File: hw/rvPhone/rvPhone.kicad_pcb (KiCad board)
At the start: 4 copper layers, 135 x 70 mm, 235 parts, among them J1 USB_OTG, J2 BATT, J202 Modem, J203 SIM_Card, J204 Motor, J205 Micro_SD_Card, J206 Camera, J3 SJ-3571N, J301 iMX8, J302 Touch, J303 Display, J304 Prog, Q1 MMBT3906, SW1 RESET, SW2 WAKE, SW201 BOOT, U1 BQ25895, U10 74HC595, U11 ICS-43434, U12 MAX98357A, U13 FT813Q, U14 FAN5333BSX, U2 TPS62293, U201 ESP32-WROOM, U202 SN74CBTLV3125, U203 TXB0104RGY, U204 TXB0104RGY, U205 DRV2605L, U206 SN74CBTLV3126, U207 TPS22917, U208 SN74LVC2G66, U209 TPS22917, U3 TPS630250, U301 SN65LVDS822_SWAP, U302 TS3DDR3812, U303 TS3DDR3812, U304 TS3DDR3812, U4 TMUX154E, U5 E310-G002, U6 IS25LP128-JBLE, U7 74HC00, U8 74HC00, U9 74HC595, X1 SiT1533, Y1 16MHz, Y2 12MHz

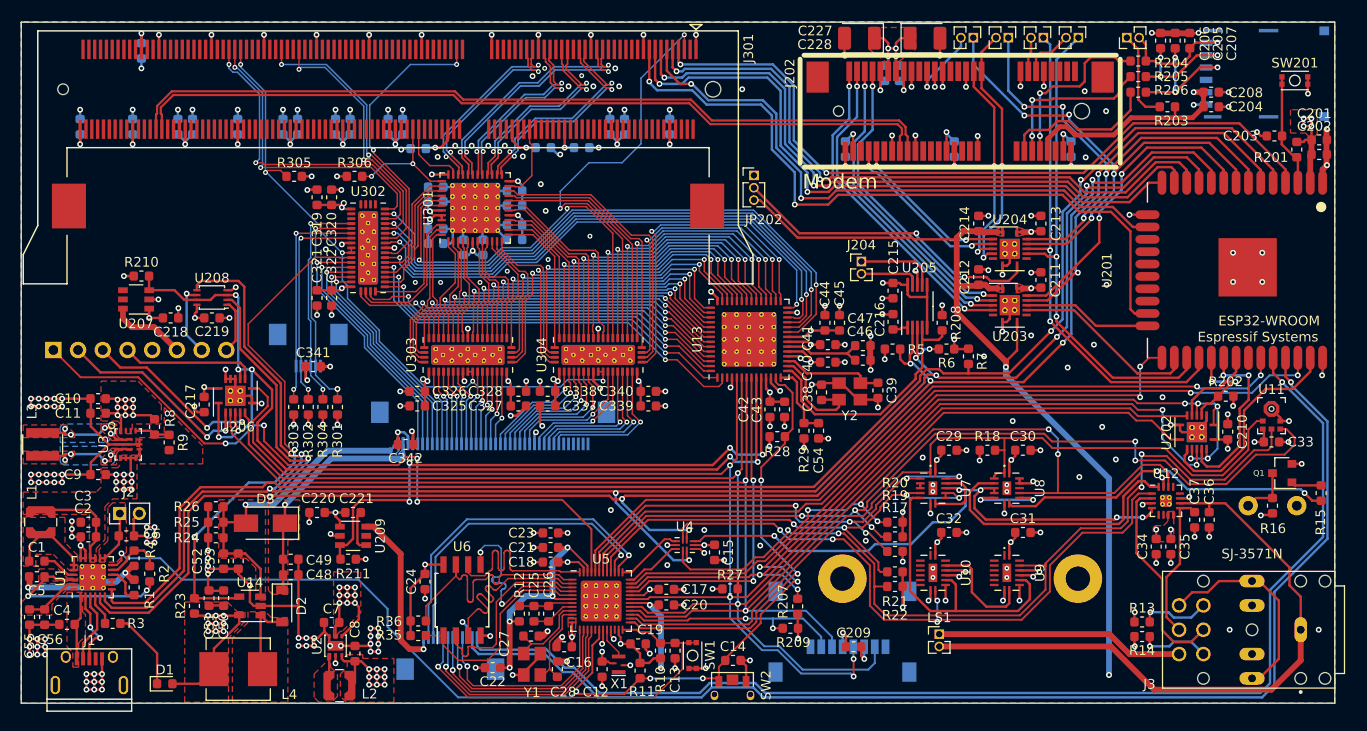
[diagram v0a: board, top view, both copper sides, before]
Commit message: stereo audio out; lvds display; LSM9DS1 added
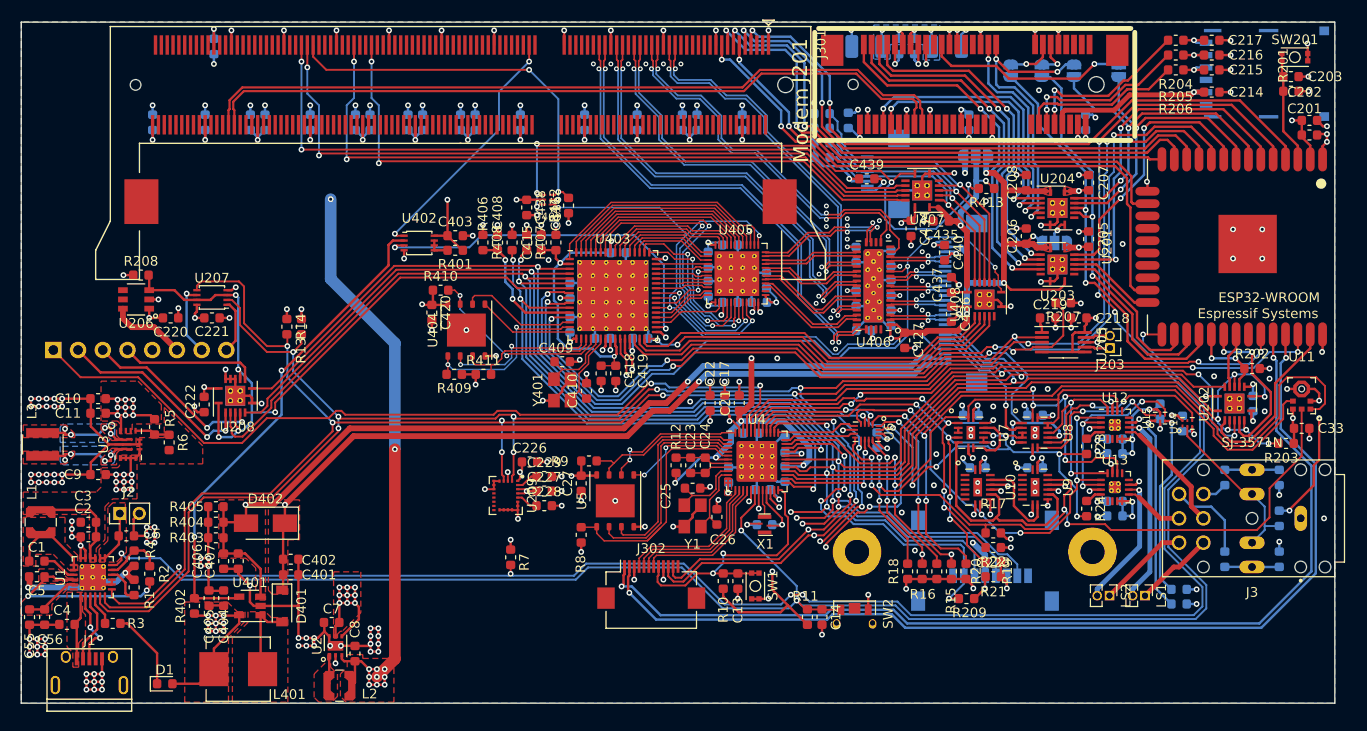
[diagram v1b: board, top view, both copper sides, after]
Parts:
- removed BZ1: Buzzer, footprints:Buzzer_12x9.5RM5.0
- removed the C15 at (168.4, 126.3)
- removed the C18 at (151.6, 127.3)
- removed the C208 at (219.5, 79.0)
- removed the C220 at (127.6, 122.2)
- removed the C221 at (131.3, 122.2)
- removed the C222 at (185.9, 77.0)
- removed the C223 at (187.4, 77.0)
- removed the C224 at (205.1, 84.8)
- removed the C225 at (193.1, 84.8)
- removed C319, C321, C325, C327, C337, C339: 1uF, Capacitor_SMD:C_0603_1608Metric
- removed C320, C322, C323, C326, C328, C329, C331, C333, C335, C338, C340, C342: 0.1uF, Capacitor_SMD:C_0603_1608Metric
- removed C324, C330, C332, C334, C336: 0.01uF, Capacitor_SMD:C_0603_1608Metric
- removed the J202 at (206.2, 81.0)
- removed the J302 at (126.7, 105.3)
- removed J303: Display, Connector_FFC-FPC:Hirose_FH12-40S-0.5SH_1x40-1MP_P0.50mm_Horizontal
- removed JP206: Q.RXD, Connector_PinHeader_1.27mm:PinHeader_1x02_P1.27mm_Vertical
- removed Q1: MMBT3906, Package_TO_SOT_SMD:SOT-23
- removed the R13 at (212.4, 133.4)
- removed the R14 at (212.4, 134.9)
- removed the R203 at (215.0, 80.5)
- removed R211, R306: 100K, Resistor_SMD:R_0603_1608Metric
- removed R302: 1K, Resistor_SMD:R_0603_1608Metric
- removed R305: 47K, Resistor_SMD:R_0603_1608Metric
- removed the U207 at (109.0, 100.3)
- removed U301: SN65LVDS822_SWAP, Package_DFN_QFN:QFN-48-1EP_7x7mm_P0.5mm_EP5.15x5.15mm_ThermalVias
- removed U302, U303, U304: TS3DDR3812, footprints:Texas_R-PWQFN-N42
- removed the U4 at (165.4, 125.5)
- removed Y2: 12MHz, footprints:TXC_7M
- added C17: 0.1uF, Capacitor_SMD:C_0603_1608Metric, F.Cu at (169.5, 111.0)
- added C209: 0.1uF, Capacitor_SMD:C_0603_1608Metric, B.Cu at (206.6, 82.1)
- added C210: 0.1uF, Capacitor_SMD:C_0603_1608Metric, B.Cu at (194.6, 82.1)
- added C211: 0.1uF, Capacitor_SMD:C_0603_1608Metric, B.Cu at (182.2, 81.9)
- added C212: 0.1uF, Capacitor_SMD:C_0603_1608Metric, B.Cu at (187.4, 74.3)
- added C213: 0.1uF, Capacitor_SMD:C_0603_1608Metric, B.Cu at (189.0, 74.3)
- added C227: 0.1uF, Capacitor_SMD:C_0603_1608Metric, F.Cu at (150.9, 120.0)
- added C228: 0.01uF, Capacitor_SMD:C_0603_1608Metric, F.Cu at (150.9, 121.5)
- added C229: 0.1uF, Capacitor_SMD:C_0603_1608Metric, F.Cu at (150.9, 118.5)
- added C26: 12pF, Capacitor_SMD:C_0603_1608Metric, F.Cu at (168.7, 122.7)
- added C40: 0.1uF, Capacitor_SMD:C_0603_1608Metric, B.Cu at (216.6, 113.0)
- added C403: 0.1uF, Capacitor_SMD:C_0603_1608Metric, F.Cu at (141.8, 93.8)
- added C409: 18pF, Capacitor_SMD:C_0603_1608Metric, F.Cu at (152.8, 106.7)
- added C41: 0.1uF, Capacitor_SMD:C_0603_1608Metric, B.Cu at (214.2, 111.8)
- added C410: 18pF, Capacitor_SMD:C_0603_1608Metric, F.Cu at (155.3, 109.7)
- added C415: 1uF, Capacitor_SMD:C_0603_1608Metric, F.Cu at (150.7, 94.5)
- added C420: 0.1uF, Capacitor_SMD:C_0603_1608Metric, F.Cu at (139.4, 101.7)
- added C421: 0.01uF, Capacitor_SMD:C_0603_1608Metric, B.Cu at (167.8, 99.2)
- added C422: 0.1uF, Capacitor_SMD:C_0603_1608Metric, B.Cu at (170.1, 100.6)
- added C423: 0.01uF, Capacitor_SMD:C_0603_1608Metric, B.Cu at (173.1, 100.6)
- added C424: 0.1uF, Capacitor_SMD:C_0603_1608Metric, B.Cu at (173.8, 98.3)
- added C425: 0.01uF, Capacitor_SMD:C_0603_1608Metric, B.Cu at (167.8, 96.2)
- added C426: 0.1uF, Capacitor_SMD:C_0603_1608Metric, B.Cu at (170.1, 94.7)
- added C427: 0.1uF, Capacitor_SMD:C_0603_1608Metric, F.Cu at (188.0, 104.5)
- added C428: 0.1uF, Capacitor_SMD:C_0603_1608Metric, B.Cu at (186.6, 102.2)
- added C429: 0.1uF, Capacitor_SMD:C_0603_1608Metric, B.Cu at (186.6, 99.1)
- added C430: 0.1uF, Capacitor_SMD:C_0603_1608Metric, B.Cu at (186.6, 96.1)
- added C431: 0.1uF, Capacitor_SMD:C_0603_1608Metric, B.Cu at (183.0, 95.7)
- added C432: 0.1uF, Capacitor_SMD:C_0603_1608Metric, B.Cu at (183.0, 100.2)
- added C433: 0.1uF, Capacitor_SMD:C_0603_1608Metric, B.Cu at (183.8, 103.5)
- added C434: 0.1uF, Capacitor_SMD:C_0603_1608Metric, F.Cu at (188.7, 93.0)
- added C435: 0.1uF, Capacitor_SMD:C_0603_1608Metric, F.Cu at (191.8, 92.2)
- added C436: 0.1uF, Capacitor_SMD:C_0603_1608Metric, F.Cu at (192.8, 101.8)
- added C437: 0.1uF, Capacitor_SMD:C_0603_1608Metric, F.Cu at (192.8, 98.8)
- added C438: 0.1uF, Capacitor_SMD:C_0603_1608Metric, F.Cu at (149.2, 90.8)
- added C440: 0.1uF, Capacitor_SMD:C_0603_1608Metric, F.Cu at (192.1, 95.5)
- added J201: Modem, footprints:Socket_mPCIe, F.Cu at (207.7, 78.2)
- added J401: Touch, Connector_FFC-FPC:Hirose_FH12-8S-0.5SH_1x08-1MP_P0.50mm_Horizontal, B.Cu at (186.0, 87.4)
- added J402: Display, Connector_FFC-FPC:Hirose_FH12-26S-0.5SH_1x26-1MP_P0.50mm_Horizontal, B.Cu at (194.0, 100.7)
- added JP401: CTP_PWR, Jumper:SolderJumper-3_P1.3mm_Open_RoundedPad1.0x1.5mm, B.Cu at (195.3, 85.6)
- added LS2: Speaker, Connector_PinHeader_1.27mm:PinHeader_1x02_P1.27mm_Vertical, F.Cu at (209.1, 130.8)
- added R23: 2K, Resistor_SMD:R_0603_1608Metric, F.Cu at (206.7, 115.4)
- added R24: 210K, Resistor_SMD:R_0603_1608Metric, F.Cu at (206.7, 121.8)
- added R25: 47K, Resistor_SMD:R_0603_1608Metric, B.Cu at (226.5, 127.0)
- added R26: 47K, Resistor_SMD:R_0603_1608Metric, B.Cu at (226.5, 118.6)
- added R28: 100K, Resistor_SMD:R_0603_1608Metric, B.Cu at (216.2, 131.6)
- added R29: 100K, Resistor_SMD:R_0603_1608Metric, B.Cu at (216.2, 130.1)
- added R401: 47K, Resistor_SMD:R_0603_1608Metric, F.Cu at (141.8, 95.2)
- added R407: 47K, Resistor_SMD:R_0603_1608Metric, F.Cu at (149.2, 94.5)
- added R409: 47K, Resistor_SMD:R_0603_1608Metric, F.Cu at (141.7, 108.0)
- added R410: 47K, Resistor_SMD:R_0603_1608Metric, F.Cu at (140.3, 99.3)
- added R411: 47K, Resistor_SMD:R_0603_1608Metric, F.Cu at (144.7, 108.0)
- added R412: 47K, Resistor_SMD:R_0603_1608Metric, F.Cu at (153.4, 90.7)
- added R413: 47K, Resistor_SMD:R_0603_1608Metric, F.Cu at (196.4, 88.9)
- added R415: 1K, Resistor_SMD:R_0603_1608Metric, B.Cu at (179.5, 84.2)
- added U14: SN74LVC1G04DRY, footprints:USON-6_1.45x1mm_P0.5mm, F.Cu at (217.1, 113.0)
- added U15: SN74LVC1G3157DRY, footprints:USON-6_1.45x1mm_P0.5mm, F.Cu at (214.2, 112.5)
- added U206: TPS22917, footprints:TPS22917, F.Cu at (109.0, 100.3)
- added U402: SN74LVC3G06DCU, Package_SO:VSSOP-8_2.4x2.1mm_P0.5mm, F.Cu at (138.1, 94.5)
- added U403: BT815Q, Package_DFN_QFN:QFN-64-1EP_9x9mm_P0.5mm_EP7.3x7.3mm_ThermalVias, F.Cu at (158.0, 99.9)
- added U404: IS25LP128-JKLE, Package_SON:WSON-8-1EP_6x5mm_P1.27mm_EP3.4x4mm, F.Cu at (142.9, 103.5)
- added U405: DS90C185, Package_DFN_QFN:QFN-48-1EP_6x6mm_P0.4mm_EP4.6x4.6mm_ThermalVias, F.Cu at (170.8, 97.7)
- added U406: TS3DV520E, footprints:Texas_R-PWQFN-N42, F.Cu at (184.8, 98.9)
- added U407: TXS0104ERGY, Package_DFN_QFN:Texas_S-PVQFN-N14_ThermalVias, F.Cu at (189.8, 89.1)
- added U408: TXS0104ERGY, Package_DFN_QFN:Texas_S-PVQFN-N14_ThermalVias, F.Cu at (196.2, 100.3)
- added U409: SN74LVC2G06DRY, footprints:USON-6_1.45x1mm_P0.5mm, F.Cu at (151.3, 90.0)
- added U5: IS25LP128-JKLE, Package_SON:WSON-8-1EP_6x5mm_P1.27mm_EP3.4x4mm, F.Cu at (158.2, 121.0)
- added Y401: 12MHz, footprints:TXC_7M, F.Cu at (152.8, 109.6)
- C12, C29, C30, C31, C32: moved to B.Cu
- C15: renamed from C16; moved to B.Cu
- C16: renamed from C17; moved to B.Cu
- C18: renamed from C19; moved to B.Cu
- C19: renamed from C20; moved to B.Cu
- C20: renamed from C21; moved to B.Cu
- C204: renamed from C210; moved to B.Cu
- C224: renamed from C227; moved to B.Cu
- C225: renamed from C228; moved to B.Cu
- C226: moved to F.Cu
- C28: value 12pF -> 0.1uF; moved to B.Cu
- C34: renamed from C35; moved to B.Cu
- C35: renamed from C34; moved to B.Cu
- C36: value 220pF -> 0.1uF; moved to B.Cu
- C37: value 220pF -> 10uF; moved to B.Cu
- C38, C39: value 18pF -> 10uF; moved to B.Cu
- C411: renamed from C40; moved to B.Cu
- C412: renamed from C41; moved to B.Cu
- C413: renamed from C42; value 27pF -> 0.1uF; moved to B.Cu
- C414: renamed from C43; moved to B.Cu
- C416: renamed from C44; value 27pF -> 0.1uF
- C417: renamed from C45; moved to B.Cu
- C418: renamed from C46; value 4.7uF -> 10uF
- J205: footprint footprints:MicroSd -> footprints:microSD
- J3: footprint footprints:CUI_SJ-3571N -> footprints:SJ-3571N
- J302: renamed from J304; moved to F.Cu
- JP201: value SIM PULL -> LEVEL EN; footprint Connector_PinHeader_1.27mm:PinHeader_1x02_P1.27mm_Vertical -> Jumper:SolderJumper-3_P1.3mm_Open_RoundedPad1.0x1.5mm; moved to B.Cu
- JP202: value LEVEL EN -> Q.DTR; footprint Connector_PinHeader_1.27mm:PinHeader_1x03_P1.27mm_Vertical -> Jumper:SolderJumper-2_P1.3mm_Open_RoundedPad1.0x1.5mm; moved to B.Cu
- JP203: value Q.DTR -> Q.RI; footprint Connector_PinHeader_1.27mm:PinHeader_1x02_P1.27mm_Vertical -> Jumper:SolderJumper-2_P1.3mm_Open_RoundedPad1.0x1.5mm; moved to B.Cu
- JP204: value Q.RI -> Q.TXD; footprint Connector_PinHeader_1.27mm:PinHeader_1x02_P1.27mm_Vertical -> Jumper:SolderJumper-2_P1.3mm_Open_RoundedPad1.0x1.5mm; moved to B.Cu
- JP205: value Q.TXD -> Q.RXD; footprint Connector_PinHeader_1.27mm:PinHeader_1x02_P1.27mm_Vertical -> Jumper:SolderJumper-2_P1.3mm_Open_RoundedPad1.0x1.5mm; moved to B.Cu
- R15, R16: value 1K -> 100K
- R27: value 47K -> 100K; moved to B.Cu
- R414: renamed from R301; value 4.7K -> 10K; moved to B.Cu
- R416: renamed from R303; moved to B.Cu
- R417: renamed from R304; moved to B.Cu
- U11: footprint footprints:TDK_ICS-43434 -> footprints:ICS-43434
- U13: value FT813Q -> MAX98357A; footprint Package_DFN_QFN:QFN-56-1EP_8x8mm_P0.5mm_EP5.6x5.6mm_ThermalVias -> footprints:TQFN-16-1EP_3x3mm_P0.5mm_EP1.23x1.23mm_ThermalVias
- U202: value SN74CBTLV3125 -> SN74CBTLV3125RGY
- U207: renamed from U208; value SN74LVC2G66 -> SN74LVC2G66DCU
- U208: renamed from U206; value SN74CBTLV3126 -> SN74CBTLV3126RGY
- U209: value TPS22917 -> LSM9DS1; footprint footprints:Texas_R-PDSO-G6 -> Package_LGA:LGA-24L_3x3.5mm_P0.43mm
- U6: value IS25LP128-JBLE -> TMUX1574RSV; footprint Package_SO:SOIJ-8_5.3x5.3mm_P1.27mm -> footprints:UQFN-16_1.8x2.6mm_P0.4mm
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- renumbered C211 to C205, C212 to C206, C213 to C207, C214 to C208, C22 to C21, C204 to C214, C205 to C215, C206 to C216, C207 to C217, C215 to C218, C216 to C219, C23 to C22, C218 to C220, C219 to C221, C217 to C222, C209 to C223, C25 to C23, C26 to C24, C27 to C25, C24 to C27, C48 to C401, C49 to C402, C50 to C404, C51 to C405, C52 to C406, C53 to C407, C54 to C408, C47 to C419, C341 to C439, D2 to D401, D3 to D402, J203 to J202, J204 to J203, J206 to J204, L4 to L401, R5 to R13, R6 to R14, R207 to R203, R208 to R207, R210 to R208, R23 to R402, R24 to R403, R25 to R404, R26 to R405, R29 to R406, R28 to R408, R8 to R5, R9 to R6, R35 to R8, R36 to R9, U5 to U4, U14 to U401
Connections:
- net BL_PWM renamed Net-(R402-Pad2)
- C217 pad 1: Net-(C207-Pad1) -> Net-(C217-Pad1)
- C28 pad 1: /XTAL_XO -> +3V3
- C34 pad 1: +3V3 -> +VSYS
- C35 pad 1: +3V3 -> +VSYS
- C36 pad 1: /SPK_VO- -> +VSYS
- C37 pad 1: /SPK_VO+ -> +VSYS
- C38 pad 2: GND -> Net-(C38-Pad2)
- C39 pad 2: GND -> Net-(C39-Pad2)
- C408 pad 1: Net-(C54-Pad1) -> Net-(C408-Pad1)
- C414 pad 1: +3V3 -> +1V8
- C416 pad 1: +3V3 -> /disp/BT81X_1V2
- C417 pad 1: +3V3 -> /disp/BT81X_1V2
- C418 pad 1: Net-(C46-Pad1) -> /disp/BT81X_1V2
- C419 pad 1: Net-(C46-Pad1) -> /disp/BT81X_1V2
- J202 pad 7: Net-(C207-Pad1) -> Net-(C217-Pad1)
- J205 pad 2: SPI1.SS0 -> SPI1.SS3
- J3 pad 1: /SPK_VO- -> GND
- J3 pad 10: Net-(J3-Pad10) -> /HP_DET
- J3 pad 11: Net-(J3-Pad11) -> /HP_DET
- J3 pad 2: Net-(J3-Pad2) -> Net-(C39-Pad1)
- J3 pad 3: Net-(J3-Pad2) -> Net-(C38-Pad1)
- J3 pad 4: Net-(J3-Pad4) -> /SPK_L+
- J3 pad 5: /SPK_GAIN -> /SPK_L_HP+
- J3 pad 6: Net-(J3-Pad6) -> Net-(C39-Pad2)
- J3 pad 7: /EAR_VO+ -> /SPK_R+
- J3 pad 8: /SPK_VO+ -> /SPK_R_HP_+
- J3 pad 9: Net-(J3-Pad2) -> Net-(C38-Pad2)
- J301 pad 129: iMX8_I2C1_SCL -> iMX8.I2C1.SCL
- J301 pad 135: iMX8_I2C1_SDA -> iMX8.I2C1.SDA
- J301 pad 149: iMX8_GPIO3_IO13 -> iMX8.GPIO3.IO13
- J301 pad 151: iMX8_GPIO3_IO12 -> iMX8.GPIO3.IO12
- J301 pad 153: iMX8_GPIO3_IO11 -> iMX8.GPIO3.IO11
- J301 pad 176: iMX8_USB1_D_P -> iMX8.USB1.D_P
- J301 pad 178: iMX8_USB1_D_N -> iMX8.USB1.D_N
- J301 pad 33: iMX8_LVDS0_CLK_P -> iMX8.LVDS0.CLK_P
- J301 pad 35: iMX8_LVDS0_CLK_N -> iMX8.LVDS0.CLK_N
- J301 pad 39: iMX8_LVDS0_A0_P -> iMX8.LVDS0.A0_P
- J301 pad 41: iMX8_LVDS0_A0_N -> iMX8.LVDS0.A0_N
- J301 pad 45: iMX8_LVDS0_A1_P -> iMX8.LVDS0.A1_P
- J301 pad 47: iMX8_LVDS0_A1_N -> iMX8.LVDS0.A1_N
- J301 pad 5: iMX8_GPIO5_IO28 -> Net-(J301-Pad5)
- J301 pad 51: iMX8_LVDS0_A2_P -> iMX8.LVDS0.A2_P
- J301 pad 53: iMX8_LVDS0_A2_N -> iMX8.LVDS0.A2_N
- J301 pad 57: iMX8_LVDS0_A3_P -> iMX8.LVDS0.A3_P
- J301 pad 58: iMX8_GPIO5_IO25 -> Net-(J301-Pad58)
- J301 pad 59: iMX8_LVDS0_A3_N -> iMX8.LVDS0.A3_N
- J301 pad 75: iMX8_PWM1 -> iMX8.PWM1
- J301 pad 88: iMX8_GPIO2_IO17 -> Net-(J301-Pad88)
- J301 pad 90: iMX8_GPIO2_IO18 -> Net-(J301-Pad90)
- J302 pad 12: TPS.VOUT -> Net-(J302-Pad12)
- JP201 pad 1: Net-(JP201-Pad1) -> GND
- JP201 pad 2: Net-(C207-Pad1) -> Net-(JP201-Pad2)
- JP202 pad 1: GND -> /periph/ESP32.U2.DTR
- JP202 pad 2: Net-(JP202-Pad2) -> /periph/Quectel.UART.DTR
- JP203 pad 1: /periph/ESP32.U2.DTR -> /periph/ESP32.U2.RI
- JP203 pad 2: /periph/Quectel.UART.DTR -> /periph/Quectel.UART.RI
- JP204 pad 1: /periph/ESP32.U2.RI -> /periph/ESP32.U2.RXD
- JP204 pad 2: /periph/Quectel.UART.RI -> /periph/Quectel.UART.TXD
- JP205 pad 1: /periph/ESP32.U2.RXD -> /periph/ESP32.U2.TXD
- JP205 pad 2: /periph/Quectel.UART.TXD -> /periph/Quectel.UART.RXD
- LS1 pad 1: /EAR_VO+ -> /SPK_L+
- LS1 pad 2: /SPK_VO- -> /SPK_L-
- R15 pad 1: Net-(Q1-Pad1) -> TMUX.GPIO0
- R15 pad 2: Net-(R15-Pad2) -> GND
- R16 pad 1: Net-(BZ1-Pad1) -> TMUX.GPIO1
- R18 pad 2: PWM0.1 -> /MIC_CLK
- R19 pad 2: PWM1.1 -> /MIC_WS
- R203 pad 2: SPI1.SS3 -> SPI1.SS0
- R204 pad 1: Net-(C207-Pad1) -> Net-(C217-Pad1)
- R207 pad 2: FT813.GPIO3 -> BT81X.GPIO3
- R208 pad 2: FT813.GPIO0 -> BT81X.GPIO0
- R209 pad 2: SPI1.SS0 -> SPI1.SS3
- R22 pad 2: /I2S_SD_OUT -> /MIC_SD
- R27 pad 1: +3V3 -> /HP_DET
- R27 pad 2: SPI1.SS2 -> +3V3
- R406 pad 2: Net-(C54-Pad1) -> Net-(C408-Pad1)
- R414 pad 2: /exp/CTP_INT -> /disp/CTP_INT
- R416 pad 2: /exp/CTP_SCL -> /disp/CTP_SCL
- R417 pad 1: /exp/CTP_RST -> /disp/CTP_RST
- U10 pad 9: /I2S_SD_IN -> /SPK_SD
- U11 pad 1: PWM1.1 -> /MIC_WS
- U11 pad 4: PWM0.1 -> /MIC_CLK
- U11 pad 6: /I2S_SD_OUT -> /MIC_SD
- U12 pad 1: /I2S_SD_IN -> /SPK_SD
- U12 pad 10: /SPK_VO- -> /SPK_L-
- U12 pad 4: /SPK_EN -> Net-(R23-Pad1)
- U12 pad 7: +3V3 -> +VSYS
- U12 pad 8: +3V3 -> +VSYS
- U12 pad 9: /SPK_VO+ -> /SPK_L_HP+
- U13 pad 1: FT813_R1 -> /SPK_SD
- U13 pad 10: FT813.GPIO1 -> /SPK_R-
- U13 pad 11: +3V3 -> GND
- U13 pad 12: Net-(U13-Pad12) -> (no net)
- U13 pad 13: GPIO_0 -> (no net)
- U13 pad 14: Net-(C54-Pad1) -> PWM2.1
- U13 pad 15: FT813.GPIO3 -> GND
- U13 pad 16: Net-(C38-Pad1) -> /SPK_CLK
- U13 pad 17: Net-(C39-Pad1) -> GND
- U13 pad 2: FT813_R0 -> /SPK_GAIN
- U13 pad 3: Net-(U13-Pad3) -> GND
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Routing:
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- added copper zone on B.Cu, net +3V3
- removed copper zone on B.Cu, net DISP_LED_A
- removed copper zone on B.Cu, net DISP_LED_K
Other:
- net class AUDIO added: clearance 0.2, trace_width 0.2, via_dia 0.6, via_drill 0.3
- net class BT81X added: clearance 0.1524, trace_width 0.1524, via_dia 0.508, via_drill 0.254
- net class CTP added: clearance 0.2, trace_width 0.2, via_dia 0.6, via_drill 0.3
- net class FE310: via_dia 0.6096 -> 0.508; via_drill 0.3048 -> 0.254

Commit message: rev2 board
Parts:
- removed the C221 at (116.8, 102.2)
- removed the C222 at (116.0, 111.1)
- removed C405, C407: 27pF, Capacitor_SMD:C_0603_1608Metric
- removed C55, C56: 22uF, Capacitor_SMD:C_0603_1608Metric
- removed J302: Prog, Connector_FFC-FPC:Hirose_FH12-12S-0.5SH_1x12-1MP_P0.50mm_Horizontal
- removed LS1, LS2: Speaker, Connector_PinHeader_1.27mm:PinHeader_1x02_P1.27mm_Vertical
- removed the R208 at (109.5, 97.8)
- removed the R414 at (179.5, 82.7)
- removed R417: 100K, Resistor_SMD:R_0603_1608Metric
- removed U209: LSM9DS1, Package_LGA:LGA-24L_3x3.5mm_P0.43mm
- added C218: 470uF, Capacitor_Tantalum_SMD:CP_EIA-7343-31_Kemet-D, B.Cu at (182.4, 74.4)
- added C219: 10nF, Capacitor_SMD:C_0603_1608Metric, F.Cu at (226.4, 78.7)
- added C230: 0.1uF, Capacitor_SMD:C_0603_1608Metric, F.Cu at (153.6, 117.9)
- added C319: 0.1uF, Capacitor_SMD:C_0603_1608Metric, F.Cu at (111.3, 86.7)
- added C42: 10uF, Capacitor_SMD:C_0603_1608Metric, F.Cu at (111.2, 127.2)
- added C43: 22uF, Capacitor_SMD:C_0805_2012Metric, F.Cu at (108.0, 124.3)
- added C44: 22uF, Capacitor_SMD:C_0805_2012Metric, F.Cu at (108.0, 126.3)
- added C441: 10uF, Capacitor_SMD:C_0603_1608Metric, F.Cu at (166.2, 102.0)
- added C45: 0.1uF, Capacitor_SMD:C_0603_1608Metric, F.Cu at (133.6, 117.8)
- added J206: Expansion, Connector_Molex:Molex_SlimStack_54722-0164_2x08_P0.50mm_Vertical, F.Cu at (168.4, 131.1)
- added J207: Camera, Connector_Molex:Molex_SlimStack_54722-0164_2x08_P0.50mm_Vertical, B.Cu at (110.6, 97.1)
- added J305: Micro_SD_Card, footprints:microSD, B.Cu at (113.3, 81.7)
- added J4: SJ-3571N, footprints:SJ-3571N, F.Cu at (223.5, 123.0)
- added J5: SPEAKER, Connector_PinHeader_2.54mm:PinHeader_1x04_P2.54mm_Vertical, F.Cu at (214.3, 132.4)
- added JP301: ALT_BOOT, Jumper:SolderJumper-2_P1.3mm_Open_RoundedPad1.0x1.5mm, B.Cu at (107.7, 91.0)
- added JP402: VOD_SEL, Jumper:SolderJumper-3_P1.3mm_Open_RoundedPad1.0x1.5mm, B.Cu at (168.4, 91.3)
- added R209: 4.7K, Resistor_SMD:R_0603_1608Metric, F.Cu at (149.9, 120.5)
- added R210: 10K, Resistor_SMD:R_0603_1608Metric, F.Cu at (151.4, 120.5)
- added R418: 100K, Resistor_SMD:R_0603_1608Metric, F.Cu at (148.9, 94.7)
- added SW202: PERST, Button_Switch_SMD:SW_SPST_PTS810, F.Cu at (225.6, 75.1)
- added TP1: BQ_INT, TestPoint:TestPoint_Pad_D1.5mm, B.Cu at (116.2, 126.6)
- added TP401: AUDIO, TestPoint:TestPoint_Pad_D1.5mm, F.Cu at (160.9, 107.2)
- added U16: SN74LVC2G07DCK, Package_TO_SOT_SMD:Texas_R-PDSO-G6, F.Cu at (136.7, 117.8)
- C10: value 22uF -> 10uF
- C11: value 22uF -> 47uF; footprint Capacitor_SMD:C_0603_1608Metric -> Capacitor_SMD:C_0805_2012Metric
- C202: value 10uF -> 22uF; footprint Capacitor_SMD:C_0603_1608Metric -> Capacitor_SMD:C_0805_2012Metric
- C203: value 0.1uF -> 1uF
- C220: value 1uF -> 10nF
- C224: value 470uF -> 0.1uF; footprint Capacitor_Tantalum_SMD:CP_EIA-3528-21_Kemet-B -> Capacitor_SMD:C_0603_1608Metric; moved to F.Cu
- C225: value 470uF -> 0.01uF; footprint Capacitor_Tantalum_SMD:CP_EIA-3528-21_Kemet-B -> Capacitor_SMD:C_0603_1608Metric; moved to F.Cu
- C228: value 0.01uF -> 0.1uF
- C25, C26: value 12pF -> 10pF
- C311, C312, C313: moved to F.Cu
- C314, C315, C316, C317, C318: footprint Capacitor_SMD:C_0603_1608Metric -> Capacitor_SMD:C_0805_2012Metric
- C409, C410: value 18pF -> 10pF
- C427, D1: moved to B.Cu
- J2: footprint Connector_PinHeader_2.00mm:PinHeader_1x02_P2.00mm_Vertical -> Connector_PinHeader_2.54mm:PinHeader_1x02_P2.54mm_Vertical
- J203: footprint Connector_PinHeader_1.27mm:PinHeader_1x02_P1.27mm_Vertical -> footprints:SolderWirePad_1x02_SMD_1x2mm; moved to B.Cu
- J204: value Camera -> Micro_SD_Card; footprint Connector_PinHeader_2.54mm:PinHeader_1x08_P2.54mm_Vertical -> footprints:microSD
- J205: value Micro_SD_Card -> Prog; footprint footprints:microSD -> Connector_FFC-FPC:Hirose_FH12-12S-0.5SH_1x12-1MP_P0.50mm_Horizontal; moved to F.Cu
- J3: value SJ-3571N -> +5V; footprint footprints:SJ-3571N -> Connector_PinHeader_2.54mm:PinHeader_1x02_P2.54mm_Vertical
- L1: footprint footprints:L_Coilcraft_LPS3015 -> Inductor_SMD:L_Vishay_IHLP-1616
- R23: value 2K -> 2.2K
- R24: value 210K -> 255K
- R28, R29: value 100K -> 50K
- R405: value R -> 68R
- R414: renamed from R415; value 1K -> R
- R415: renamed from R416; value 1K -> R
- R7: value 10K -> 100K
- SW1, SW201: footprint footprints:Panasonic_EVPBB -> Button_Switch_SMD:SW_SPST_PTS810
- SW2: footprint footprints:Panasonic_EVPAK -> footprints:Panasonic_EVPAE
- U14: value SN74LVC1G04DRY -> SN74LVC1G04DCK; footprint footprints:USON-6_1.45x1mm_P0.5mm -> footprints:Texas_R-PDSO-G5
- U15: value SN74LVC1G3157DRY -> SN74LVC1G3157DCK; footprint footprints:USON-6_1.45x1mm_P0.5mm -> Package_TO_SOT_SMD:Texas_R-PDSO-G6
- U205: value DRV2605L -> DRV2605LDGS
- U206: value TPS22917 -> LSM9DS1; footprint footprints:TPS22917 -> Package_LGA:LGA-24L_3x3.5mm_P0.43mm
- U207: value SN74LVC2G66DCU -> FT230XQ; footprint Package_SO:VSSOP-8_2.4x2.1mm_P0.5mm -> Package_DFN_QFN:QFN-16-1EP_4x4mm_P0.65mm_EP2.1x2.1mm
- U208: value SN74CBTLV3126RGY -> TMUX154ERSW; footprint Package_DFN_QFN:Texas_S-PVQFN-N14_ThermalVias -> footprints:UQFN-10_1.4x1.8mm_P0.4mm
- U4: value E310-G002 -> FE310-G002
- U403: value BT815Q -> BT817Q; footprint Package_DFN_QFN:QFN-64-1EP_9x9mm_P0.5mm_EP7.3x7.3mm_ThermalVias -> Package_DFN_QFN:QFN-64-1EP_9x9mm_P0.5mm_EP6x6mm_ThermalVias
- U406: value TS3DV520E -> TS3DV520ERUA
- U409: value SN74LVC2G06DRY -> SN74LVC2G06DCK; footprint footprints:USON-6_1.45x1mm_P0.5mm -> Package_TO_SOT_SMD:Texas_R-PDSO-G6
- moved C220 114.1 mm to (223.0, 73.8), turned to 270 degrees
- moved J3 112.1 mm to (111.9, 130.9), turned to 0 degrees
- moved U206 98.2 mm to (201.8, 132.3), turned to 0 degrees
- moved J204 98.0 mm to (196.1, 127.3), turned to 180 degrees
- moved C225 57.5 mm to (203.4, 128.4), turned to 90 degrees
- moved C224 55.0 mm to (201.9, 128.4), turned to 90 degrees
- moved C226 52.2 mm to (200.4, 128.4), turned to 90 degrees
- moved J205 49.1 mm to (147.3, 130.4), turned to 0 degrees
- moved C227 46.5 mm to (196.6, 129.0)
- moved C11 39.6 mm to (141.9, 126.5)
- moved L3 39.1 mm to (137.8, 122.6), turned to 0 degrees
- moved C10 38.8 mm to (139.6, 128.2)
- moved C8 35.8 mm to (110.5, 107.8), turned to 180 degrees
- moved R5 35.7 mm to (140.5, 133.3)
- moved U207 35.0 mm to (146.5, 118.7), turned to 270 degrees
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- renumbered C218 to C221, C219 to C222, JP205 to JP204, JP204 to JP205, R209 to R208
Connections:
- net /disp/DISP_LVDS_CLK_N renamed /disp/DISP_LVDS_CLKN
- net /disp/DISP_LVDS_CLK_P renamed /disp/DISP_LVDS_CLKP
- net /disp/DS90_LVDS_A0_N renamed /disp/DS90_LVDS_A0N
- net /disp/DS90_LVDS_A0_P renamed /disp/DS90_LVDS_A0P
- net /disp/DS90_LVDS_A1_N renamed /disp/DS90_LVDS_A1N
- net /disp/DS90_LVDS_A1_P renamed /disp/DS90_LVDS_A1P
- net /disp/DS90_LVDS_A2_N renamed /disp/DS90_LVDS_A2N
- net /disp/DS90_LVDS_A2_P renamed /disp/DS90_LVDS_A2P
- net /disp/DS90_LVDS_A3_N renamed /disp/DS90_LVDS_A3N
- net /disp/DS90_LVDS_A3_P renamed /disp/DS90_LVDS_A3P
- net /disp/DS90_LVDS_CLK_N renamed /disp/DS90_LVDS_CLKN
- net /disp/DS90_LVDS_CLK_P renamed /disp/DS90_LVDS_CLKP
- net Net-(C203-Pad1) renamed /periph/ESP32.EN
- net RESET renamed /RESET
- net iMX8.LVDS0.A0_N renamed iMX8.LVDS0.A0N
- net iMX8.LVDS0.A0_P renamed iMX8.LVDS0.A0P
- net iMX8.LVDS0.A1_N renamed iMX8.LVDS0.A1N
- net iMX8.LVDS0.A1_P renamed iMX8.LVDS0.A1P
- net iMX8.LVDS0.A2_N renamed iMX8.LVDS0.A2N
- net iMX8.LVDS0.A2_P renamed iMX8.LVDS0.A2P
- net iMX8.LVDS0.A3_N renamed iMX8.LVDS0.A3N
- net iMX8.LVDS0.A3_P renamed iMX8.LVDS0.A3P
- net iMX8.LVDS0.CLK_N renamed iMX8.LVDS0.CLKN
- net iMX8.LVDS0.CLK_P renamed iMX8.LVDS0.CLKP
- C220 pad 1: +3V3 -> /periph/PERST
- C225 pad 1: +3V3 -> Net-(C225-Pad1)
- C226 pad 1: +3V3 -> Net-(C226-Pad1)
- C228 pad 1: Net-(C228-Pad1) -> +3V3
- C229 pad 1: Net-(C229-Pad1) -> +3V3
- C427 pad 1: +1V8 -> +3V3
- C428 pad 1: +1V8 -> +3V3
- C429 pad 1: +1V8 -> +3V3
- C430 pad 1: +1V8 -> +3V3
- C431 pad 1: +1V8 -> +3V3
- C432 pad 1: +1V8 -> +3V3
- C433 pad 1: +1V8 -> +3V3
- C439 pad 1: +3V3 -> +VCTP
- J1 pad 2: Net-(J1-Pad2) -> USB_D-
- J1 pad 3: Net-(J1-Pad3) -> USB_D+
- J1 pad 6: Net-(J1-Pad6) -> GND
- J201 pad 22: Net-(J201-Pad22) -> /periph/PERST
- J204 pad 1: GPIO_23 -> Net-(J204-Pad1)
- J204 pad 2: /periph/CAM.MOSI -> SPI1.SS3
- J204 pad 3: /periph/CAM.MISO -> SPI1.MOSI
- J204 pad 4: /periph/CAM.SCK -> +3V3
- J204 pad 5: GND -> SPI1.SCK
- J204 pad 6: /periph/CAM.PWR -> GND
- J204 pad 7: /periph/CAM.SDA -> SPI1.MISO
- J204 pad 8: /periph/CAM.SCL -> Net-(J204-Pad8)
- J205 pad 1: Net-(J205-Pad1) -> ESP32.UART0.RXD
- J205 pad 2: SPI1.SS3 -> ESP32.UART0.TXD
- J205 pad 3: SPI1.MOSI -> GND
- J205 pad 4: +3V3 -> JTAG_TCK
- J205 pad 5: SPI1.SCK -> JTAG_TDO
- J205 pad 6: GND -> JTAG_TMS
- J205 pad 7: SPI1.MISO -> JTAG_TDI
- J205 pad 8: Net-(J205-Pad8) -> JTAG_TRST_N
- J205 pad 9: Net-(J205-Pad9) -> GND
- J3 pad 1: GND -> /BQ_PMID
- J3 pad 2: Net-(C39-Pad1) -> GND
- J301 pad 129: iMX8.I2C1.SCL -> Net-(J301-Pad129)
- J301 pad 135: iMX8.I2C1.SDA -> Net-(J301-Pad135)
- J301 pad 149: iMX8.GPIO3.IO13 -> Net-(J301-Pad149)
- J301 pad 151: iMX8.GPIO3.IO12 -> Net-(J301-Pad151)
- J301 pad 153: iMX8.GPIO3.IO11 -> Net-(J301-Pad153)
- J301 pad 185: Net-(J301-Pad185) -> /exp/ALT_BOOT
- J301 pad 200: Net-(J301-Pad200) -> iMX8.PWM1
- J301 pad 3: Net-(J301-Pad3) -> iMX8.GPIO5.IO29
- J301 pad 43: Net-(J301-Pad43) -> iMX8.I2C3.SCL
- J301 pad 49: Net-(J301-Pad49) -> iMX8.I2C3.SDA
- J301 pad 5: Net-(J301-Pad5) -> iMX8.GPIO5.IO28
- J301 pad 61: Net-(J301-Pad61) -> GND
- J301 pad 67: Net-(J301-Pad67) -> GND
- J301 pad 75: iMX8.PWM1 -> Net-(J301-Pad75)
- J301 pad 76: Net-(J301-Pad76) -> iMX8.GPIO3.IO7
- J301 pad 80: Net-(J301-Pad80) -> /exp/SD2_CLK
- J301 pad 82: Net-(J301-Pad82) -> /exp/SD2_CMD
- J301 pad 84: Net-(J301-Pad84) -> /exp/SD2_DAT0
- J301 pad 86: Net-(J301-Pad86) -> /exp/SD2_DAT1
- J301 pad 88: Net-(J301-Pad88) -> /exp/SD2_DAT2
- J301 pad 90: Net-(J301-Pad90) -> /exp/SD2_DAT3
- J401 pad 3: +3V3 -> +VCTP
- J402 pad 19: SPI1.MISO -> DISP_CS
- J402 pad 20: SPI1.MOSI -> SPI1.SCK
- J402 pad 21: SPI1.SCK -> SPI1.MOSI
- J402 pad 22: DISP_CS -> SPI1.MISO
- R412 pad 2: iMX8.GPIO3.IO13 -> iMX8.GPIO3.IO7
- R414 pad 1: +3V3 -> +VCTP
- R415 pad 1: +3V3 -> +VCTP
- R7 pad 2: ESP32.IO39 -> JTAG_TRST_N
- U1 pad 12: WAKE -> /BQ_QON
- U1 pad 2: Net-(J1-Pad3) -> Net-(U1-Pad2)
- U1 pad 23: Net-(C55-Pad1) -> /BQ_PMID
- U1 pad 3: Net-(J1-Pad2) -> Net-(U1-Pad2)
- U1 pad 7: ESP32.IO39 -> /BQ_INT
- U1 pad 8: GND -> +VSYS
- U14 pad 5: Net-(U14-Pad5) -> +3V3
- U201 pad 10: TMUX.I2C0.SCL -> Net-(U201-Pad10)
- U201 pad 11: TMUX.I2C0.SDA -> Net-(U201-Pad11)
- U201 pad 34: ESP32.RXD0 -> ESP32.UART0.RXD
- U201 pad 35: ESP32.TXD0 -> ESP32.UART0.TXD
- U201 pad 5: ESP32.IO39 -> Net-(U201-Pad5)
- U206 pad 2: GND -> TMUX.I2C0.SCL
- U206 pad 3: BT81X.GPIO0 -> +3V3
- U206 pad 4: Net-(U206-Pad4) -> TMUX.I2C0.SDA
- U206 pad 5: Net-(U206-Pad5) -> +3V3
- U206 pad 6: /periph/CAM.PWR -> +3V3
- U207 pad 1: /periph/CAM.SCL -> +3V3
- U207 pad 2: TMUX.I2C0.SCL -> /periph/USB_RXD
- U207 pad 3: BT81X.GPIO0 -> GND
- U207 pad 5: TMUX.I2C0.SDA -> Net-(U207-Pad5)
- U207 pad 6: /periph/CAM.SDA -> USB_D+
- U207 pad 7: BT81X.GPIO0 -> USB_D-
- U208 pad 1: BT81X.GPIO0 -> UART0.RXD
- U208 pad 10: BT81X.GPIO0 -> /periph/USB_CBUS1
- U208 pad 2: /periph/CAM.MOSI -> ESP32.UART0.RXD
- U208 pad 3: SPI1.MOSI -> /periph/USB_TXD
- U208 pad 4: BT81X.GPIO0 -> GND
- U208 pad 5: /periph/CAM.MISO -> /periph/USB_RXD
- U208 pad 6: SPI1.MISO -> ESP32.UART0.TXD
- U208 pad 7: GND -> UART0.TXD
- U208 pad 8: SPI1.SCK -> /periph/USB_CBUS0
- U208 pad 9: /periph/CAM.SCK -> +3V3
- U4 pad 38: UART0.RX -> UART0.RXD
- U4 pad 39: UART0.TX -> UART0.TXD
- U406 pad 1: +1V8 -> +3V3
- U406 pad 13: +1V8 -> +3V3
- U406 pad 22: +1V8 -> +3V3
- U406 pad 31: +1V8 -> +3V3
- U406 pad 4: +1V8 -> +3V3
- U406 pad 40: +1V8 -> +3V3
- U406 pad 7: +1V8 -> +3V3
- U407 pad 10: iMX8.GPIO3.IO11 -> iMX8.GPIO5.IO29
- U407 pad 11: iMX8.GPIO3.IO12 -> iMX8.GPIO5.IO28
- U407 pad 12: iMX8.I2C1.SDA -> iMX8.I2C3.SDA
- U407 pad 13: iMX8.I2C1.SCL -> iMX8.I2C3.SCL
- U409 pad 3: iMX8.GPIO3.IO13 -> iMX8.GPIO3.IO7
- U7 pad 10: GPIO_18 -> Net-(U7-Pad10)
- U7 pad 11: /SPK_EN -> Net-(U7-Pad10)
- U7 pad 12: Net-(U7-Pad12) -> GPIO_18
- U7 pad 13: PWM1.2 -> GPIO_18
- U7 pad 8: Net-(U7-Pad12) -> /SPK_EN
- U7 pad 9: GPIO_18 -> PWM1.2
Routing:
- net ESP32.IO39: track 198.5 -> 0.00 mm, vias 7 -> 0
- net ESP32.UART0.TXD: track 0.00 -> 135.8 mm, vias 0 -> 4
- net ESP32.UART0.RXD: track 0.00 -> 135.2 mm, vias 0 -> 4
- net ESP32.TXD0: track 103.9 -> 0.00 mm, vias 2 -> 0
- net ESP32.RXD0: track 103.3 -> 0.00 mm, vias 2 -> 0
- net UART0.TXD: track 0.00 -> 88.3 mm, vias 0 -> 6
- net UART0.RXD: track 0.00 -> 87.9 mm, vias 0 -> 6
- net iMX8.GPIO3.IO11: track 74.6 -> 0.00 mm, vias 2 -> 0
- net iMX8.GPIO3.IO12: track 73.9 -> 0.00 mm, vias 2 -> 0
- net +1V8: track 201.3 -> 127.8 mm, vias 33 -> 23
- net iMX8.I2C1.SDA: track 71.2 -> 0.00 mm, vias 2 -> 0
- net iMX8.I2C1.SCL: track 68.3 -> 0.00 mm, vias 2 -> 0
- net +3V3: track 196.3 -> 247.0 mm, vias 73 -> 76
- net /periph/PERST: track 0.00 -> 43.3 mm, vias 0 -> 2
- net USB_D+: track 0.00 -> 43.2 mm, vias 0 -> 2
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- added copper zone on B.Cu, net +1V8
- added copper zone on F.Cu, net +VCTP
- added copper zone on F.Cu, net /BQ_PMID
- added copper zone on F.Cu, net /SPK_L_HP+
- added copper zone on F.Cu, net /SPK_R_HP_+
- added copper zone on B.Cu, net DISP_LED_A
- added copper zone on B.Cu, net DISP_LED_K
- added copper zone on PWR, net GND
- added copper zone on B.Cu, net Net-(C6-Pad1)
- removed copper zone on F.Cu, net Net-(C5-Pad1)
- removed copper zone on F.Cu, net Net-(C55-Pad1)
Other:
- board size 135 x 70 mm -> 126 x 63 mm
- net class MODEM_USB removed
- net class USB added: clearance 0.2, trace_width 0.2, via_dia 0.6, via_drill 0.3
- net class USB2DIFF added: clearance 0.1524, trace_width 0.2288, via_dia 0.508, via_drill 0.254
- rule pad_to_mask_clearance: 0.045 -> 0.05

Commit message: temp commit for merge
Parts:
- removed C435, C436, C437, C438, C439, C440: 0.1uF, Capacitor_SMD:C_0603_1608Metric
- removed J305: Micro_SD_Card, footprints:microSD
- removed JP401: CTP_PWR, Jumper:SolderJumper-3_P1.3mm_Open_RoundedPad1.0x1.5mm
- removed R412, R413: 47K, Resistor_SMD:R_0603_1608Metric
- removed R414, R415: R, Resistor_SMD:R_0603_1608Metric
- removed U408: TXS0104ERGY, Package_DFN_QFN:Texas_S-PVQFN-N14_ThermalVias
- removed U409: SN74LVC2G06DCK, Package_TO_SOT_SMD:Texas_R-PDSO-G6
- added C228: 22uF, Capacitor_SMD:C_0805_2012Metric, F.Cu at (191.3, 123.7)
- added C320: 22uF, Capacitor_SMD:C_0805_2012Metric, B.Cu at (116.3, 92.0)
- added J302: Micro_SD_Card_Det, footprints:Molex_MicroSD-5027740891, B.Cu at (120.8, 72.3)
- added J303: Spacer, footprints:Spacer, F.Cu at (120.4, 120.9)
- added J403: Spacer, footprints:Spacer, B.Cu at (222.9, 100.0)
- added JP302: USB_ID, Jumper:SolderJumper-2_P1.3mm_Open_RoundedPad1.0x1.5mm, B.Cu at (108.7, 91.2)
- added R23: 100K, Resistor_SMD:R_0603_1608Metric, F.Cu at (145.9, 94.7)
- added R24: 100K, Resistor_SMD:R_0603_1608Metric, F.Cu at (144.4, 94.7)
- added R25: 100K, Resistor_SMD:R_0603_1608Metric, F.Cu at (147.4, 94.7)
- added R301: 100K, Resistor_SMD:R_0603_1608Metric, B.Cu at (120.8, 90.3)
- added R31: 100K, Resistor_SMD:R_0603_1608Metric, F.Cu at (163.8, 106.3)
- added SW301: iMX8_ALT_BOOT, Button_Switch_SMD:SW_SPST_PTS810, F.Cu at (131.7, 122.5)
- added SW302: iMX8_RST, Button_Switch_SMD:SW_SPST_PTS810, F.Cu at (131.7, 126.2)
- added SW303: iMX8_PWR, Button_Switch_SMD:SW_SPST_PTS810, F.Cu at (131.7, 129.9)
- added TP2: PMU_OUT0, TestPoint:TestPoint_Pad_D1.5mm, F.Cu at (177.2, 121.8)
- C14: value 10nF -> 22uF; footprint Capacitor_SMD:C_0603_1608Metric -> Capacitor_SMD:C_0805_2012Metric; moved to B.Cu
- C219: value 10nF -> 0.1uF
- C220: value 10nF -> 0.1uF; moved to B.Cu
- C319, R3: moved to B.Cu
- J1: footprint footprints:USB_Micro-B -> footprints:GCT_MicroUSB-USB3080
- J201: footprint footprints:Socket_mPCIe -> footprints:TE_mPCIe-1775862
- J204: value Micro_SD_Card -> Micro_SD_Card_Det; footprint footprints:microSD -> footprints:Molex_MicroSD-5027740891
- J301: footprint footprints:Socket_SODIMM_DDR3_TE_2013289 -> footprints:TE_SODIMMDDR3-2013289
- J401: value Touch -> Display; footprint Connector_FFC-FPC:Hirose_FH12-8S-0.5SH_1x08-1MP_P0.50mm_Horizontal -> Connector_Molex:Molex_SlimStack_54722-0304_2x15_P0.50mm_Vertical
- J402: value Display -> Spacer; footprint Connector_FFC-FPC:Hirose_FH12-26S-0.5SH_1x26-1MP_P0.50mm_Horizontal -> footprints:Spacer
- JP201: value LEVEL EN -> SIMCom_EN
- JP301: value ALT_BOOT -> USB_VBUS
- L2: footprint footprints:L_Coilcraft_LPS3015 -> footprints:Coilcraft-LPS3015
- L3: footprint footprints:L_Coilcraft_XAL40 -> footprints:Coilcraft-XAL40
- L401: footprint footprints:L_Murata_LQH66SN -> footprints:Murata-LQH66SN
- SW201: value BOOT -> ESP32_RST
- SW202: value PERST -> MODEM_RST
- U10, U9: footprint footprints:74HC595BQ115 -> footprints:DHVQFN-16_2.5x3.5mm_P0.5mm_EP1.0x2.0mm
- U202, U203, U204: footprint Package_DFN_QFN:Texas_S-PVQFN-N14_ThermalVias -> footprints:Texas_S-PVQFN-N14_ThermalVias
- U407: value TXS0104ERGY -> TMUX1574RSV; footprint Package_DFN_QFN:Texas_S-PVQFN-N14_ThermalVias -> footprints:UQFN-16_1.8x2.6mm_P0.4mm
- U7, U8: footprint footprints:74HC00BQ115 -> footprints:DHVQFN-14_2.5x3.0mm_P0.5mm_EP1.0x1.5mm
- moved C45 61.8 mm to (192.9, 134.8)
- moved U16 61.8 mm to (196.0, 134.8)
- moved R7 58.1 mm to (195.9, 132.7), turned to 0 degrees
- moved SW1 50.2 mm to (195.0, 138.2)
- moved R10 48.7 mm to (198.6, 138.1)
- moved C14 42.6 mm to (139.5, 89.5)
- moved J205 39.1 mm to (186.1, 135.3)
- moved C8 31.8 mm to (128.0, 134.2)
- moved L2 31.8 mm to (131.2, 135.8)
- moved U2 31.8 mm to (127.2, 136.2)
- moved C7 31.8 mm to (124.9, 136.4)
- moved J402 31.3 mm to (222.9, 89.3), turned to 0 degrees
- moved C220 31.2 mm to (192.2, 78.2), turned to 180 degrees
- moved C13 26.8 mm to (176.9, 125.2)
- moved R6 26.2 mm to (164.4, 135.1), turned to 270 degrees
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- renumbered C228 to C229, C229 to C230, C230 to C231, R23 to R26, R24 to R27, R25 to R28, R26 to R29, R27 to R30, R28 to R32, R29 to R33
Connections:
- net Net-(TP401-Pad1) renamed /disp/BT81X_AUDIO
- net Net-(U4-Pad17) renamed /AON_PMU_OUT_1
- C14 pad 1: WAKE -> +1V8
- J1 pad 6: GND -> Net-(J1-Pad6)
- J204 pad 2: SPI1.SS3 -> GPIO_0
- J204 pad 9: GND -> Net-(J204-Pad9)
- J206 pad 10: UART0.TXD -> TMUX.I2C0.SCL
- J206 pad 11: SPI1.MOSI -> GND
- J206 pad 13: SPI1.MISO -> UART0.TXD
- J206 pad 14: TMUX.I2C0.SDA -> TMUX.GPIO1
- J206 pad 15: SPI1.SCK -> UART0.RXD
- J206 pad 16: TMUX.I2C0.SCL -> TMUX.GPIO0
- J206 pad 5: TMUX.GPIO0 -> SPI1.MOSI
- J206 pad 7: TMUX.GPIO1 -> SPI1.MISO
- J206 pad 8: UART0.RXD -> TMUX.I2C0.SDA
- J206 pad 9: GND -> SPI1.SCK
- J207 pad 1: GPIO_23 -> TMUX.I2C0.SCL
- J207 pad 3: TMUX.I2C0.SCL -> TMUX.I2C0.SDA
- J207 pad 5: TMUX.I2C0.SDA -> SPI1.SS2
- J301 pad 165: Net-(J301-Pad165) -> /exp/POWER
- J301 pad 171: Net-(J301-Pad171) -> /exp/RESET
- J301 pad 174: Net-(J301-Pad174) -> iMX8.USB1.ID
- J301 pad 180: Net-(J301-Pad180) -> iMX8.USB1.VBUS
- J301 pad 61: GND -> /exp/SD2_DET
- J301 pad 7: ESP32.IO36 -> ESP32.IO26
- J301 pad 76: iMX8.GPIO3.IO7 -> Net-(J301-Pad76)
- J401 pad 1: GND -> +3V3
- J401 pad 3: +VCTP -> +1V8
- J401 pad 4: /disp/CTP_SCL -> /disp/DISP_LVDS_A0N
- J401 pad 5: /disp/CTP_SDA -> /disp/CTP_SCL
- J401 pad 6: /disp/CTP_INT -> /disp/DISP_LVDS_A0P
- J401 pad 7: /disp/CTP_RST -> /disp/CTP_SDA
- J402 pad 1: +3V3 -> GND
- JP301 pad 1: /exp/ALT_BOOT -> +3V3
- JP301 pad 2: +3V3 -> iMX8.USB1.VBUS
- R208 pad 2: SPI1.SS3 -> GPIO_0
- R407 pad 2: SPI1.SS2 -> SPI1.SS3
- R408 pad 2: GPIO_0 -> GPIO_23
- SW2 pad 1: WAKE -> GND
- SW2 pad 2: GND -> WAKE
- U201 pad 11: Net-(U201-Pad11) -> ESP32.IO26
- U201 pad 4: ESP32.IO36 -> Net-(U201-Pad4)
- U4 pad 22: Net-(U4-Pad22) -> /AON_PMU_OUT_0
- U403 pad 11: GPIO_0 -> GPIO_23
- U403 pad 6: SPI1.SS2 -> SPI1.SS3
- U407 pad 1: +VCTP -> TMUX.I2C0.SCL
- U407 pad 10: iMX8.GPIO5.IO29 -> /disp/CTP_RST
- U407 pad 11: iMX8.GPIO5.IO28 -> TMUX.GPIO0
- U407 pad 12: iMX8.I2C3.SDA -> iMX8.GPIO5.IO29
- U407 pad 13: iMX8.I2C3.SCL -> GND
- U407 pad 15: GND -> BT81X.DISP
- U407 pad 3: /disp/CTP_SDA -> iMX8.I2C3.SDA
- U407 pad 4: /disp/CTP_INT -> TMUX.I2C0.SDA
- U407 pad 5: /disp/CTP_RST -> /disp/CTP_SDA
- U407 pad 6: Net-(U407-Pad6) -> GND
- U407 pad 7: GND -> /disp/CTP_INT
- U407 pad 8: /disp/iMX8_CTP_EN -> TMUX.GPIO1
- U407 pad 9: Net-(U407-Pad9) -> iMX8.GPIO5.IO28
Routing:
- net /exp/RESET: track 0.00 -> 73.1 mm, vias 0 -> 2
- net ESP32.IO36: track 69.0 -> 0.00 mm, vias 2 -> 0
- net /BQ_QON: track 28.3 -> 93.0 mm
- net ESP32.IO26: track 0.00 -> 57.6 mm, vias 0 -> 2
- net /exp/SD2_DET: track 0.00 -> 53.6 mm, vias 0 -> 1
- net /disp/iMX8_CTP_EN: track 49.8 -> 0.00 mm, vias 4 -> 0
- net +1V8: track 127.8 -> 175.7 mm, vias 23 -> 28
- net +VCTP: track 46.4 -> 0.00 mm, vias 3 -> 0
- net TMUX.GPIO0: track 46.3 -> 90.1 mm, vias 4 -> 5
- net TMUX.GPIO1: track 37.9 -> 81.0 mm, vias 4 -> 5
- net BT81X.CTP.RST: track 41.7 -> 0.00 mm
- net BT81X.CTP.INT: track 40.3 -> 0.00 mm
- net BT81X.CTP.SDA: track 38.3 -> 0.00 mm, vias 2 -> 0
- net /exp/POWER: track 0.00 -> 38.2 mm, vias 0 -> 1
- net BT81X.CTP.SCL: track 38.0 -> 0.00 mm
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- removed copper zone on F.Cu, net +VCTP
- removed copper zone on B.Cu, net DISP_LED_K
- removed copper zone on B.Cu, net Net-(C6-Pad1)
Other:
- board size 126 x 63 mm -> 126 x 68 mm
